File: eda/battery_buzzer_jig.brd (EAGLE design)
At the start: 47 x 26.7 mm, 12 parts, among them J2 AVR_SPI_PRG_6PTH

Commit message: Much tidying in pie.lbr
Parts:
- moved J2 0.54 mm to (4.45, 1.91)
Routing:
- net SCK: track 20.3 -> 20.8 mm
- net MOSI: track 22.0 -> 22.6 mm
- net MISO: track 16.7 -> 17.3 mm
- net RESET: track 37.9 -> 38.4 mm

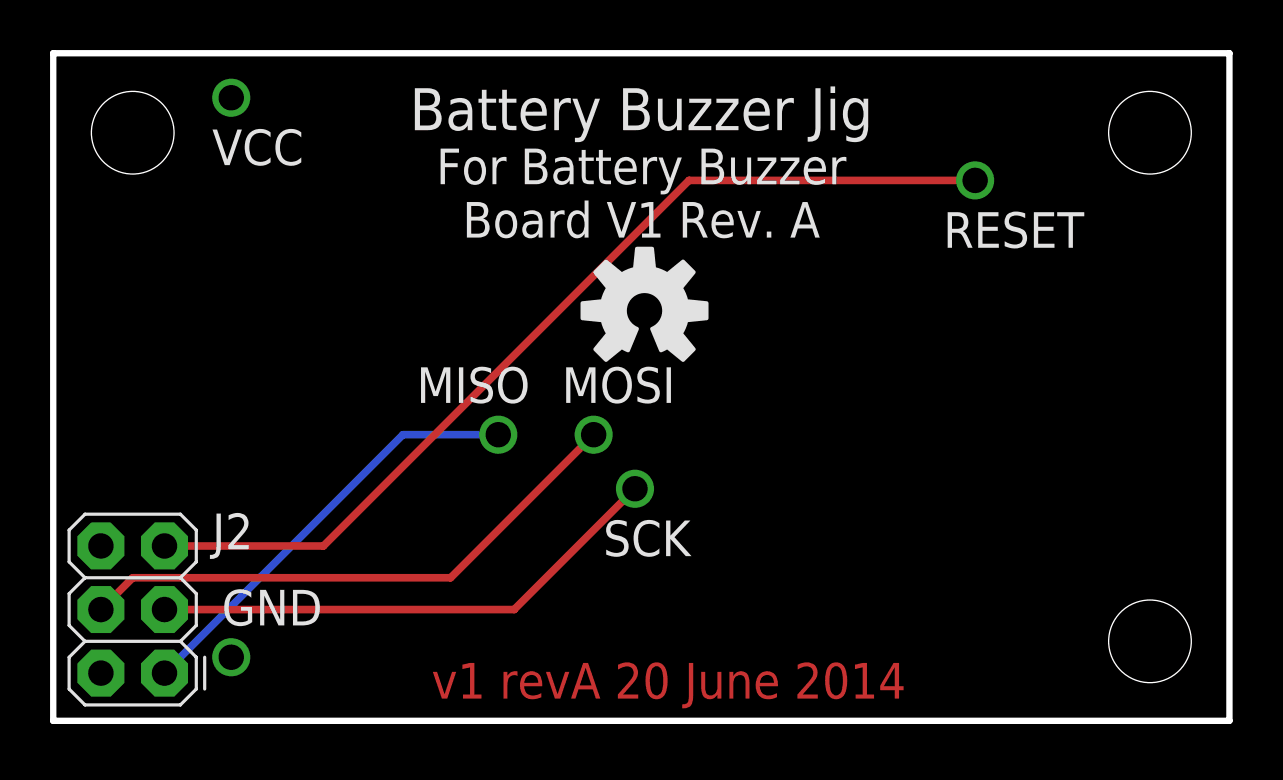
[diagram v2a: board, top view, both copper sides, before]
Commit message: All jigs probe vias accessible after populating.
Also changed "VCC" signal name on jigs to "5V" to match boards.
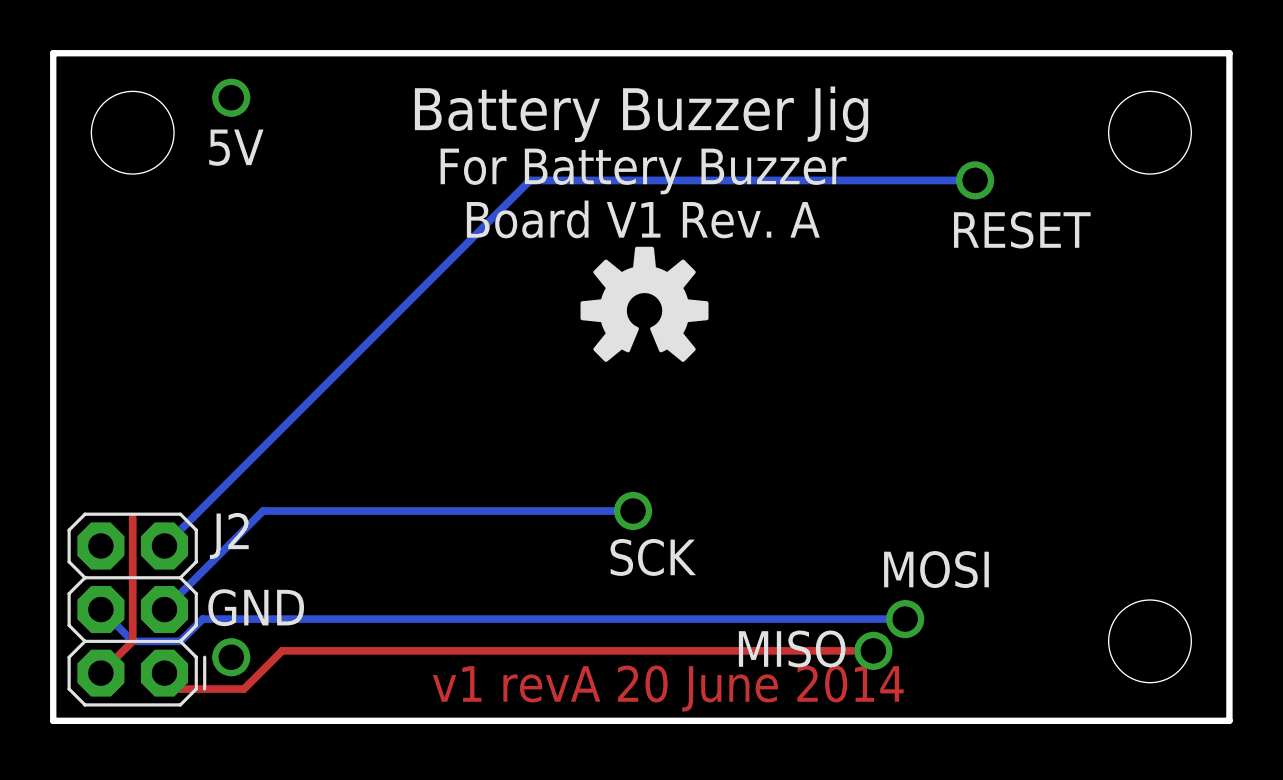
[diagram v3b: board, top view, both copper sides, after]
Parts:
- moved MISO 17.3 mm to (32.8, 2.79)
- moved MOSI 14.5 mm to (34.0, 4.06)
- moved SCK 0.89 mm to (23.2, 8.38)
- renumbered VCC to 5V
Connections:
- net VCC renamed 5V
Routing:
- net MISO: track 17.3 -> 29.2 mm
- net MOSI: track 22.6 -> 33.0 mm
- net 5V: track 0.00 -> 6.75 mm
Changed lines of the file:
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@@
 <text x="23.495" y="22.86" size="1.4224" layer="21" font="vector" ratio="15" align="top-center">For Battery Buzzer
 Board V1 Rev. A</text>
-<text x="15.113" y="0.889" size="1.4224" layer="1" font="vector" ratio="15">v1 revA 20 June 2014</text>
+<text x="15.113" y="0.762" size="1.4224" layer="1" font="vector" ratio="15">v1 revA 20 June 2014</text>
 </plain>
 <attributes>
@@
 <attribute name="PIE-INT-REF-NUM" value="BULK-STOCK" x="4.445" y="1.905" size="1.778" layer="27" rot="R90" display="off"/>
 </element>
-<element name="MISO" library="pie" package="POGO_PIN_394" value="" x="17.78" y="11.43" smashed="yes">
-<attribute name="NAME" x="19.05" y="12.7" size="1.4224" layer="25" font="vector" ratio="15" align="bottom-right"/>
-<attribute name="VALUE" x="16.51" y="8.89" size="1.27" layer="27" font="vector"/>
-<attribute name="PIE-INT-REF-NUM" value="POGO-PIN" x="17.78" y="11.43" size="1.778" layer="27" display="off"/>
-</element>
-<element name="SCK" library="pie" package="POGO_PIN_394" value="" x="23.241" y="9.271" smashed="yes">
-<attribute name="NAME" x="21.971" y="8.001" size="1.4224" layer="25" font="vector" ratio="15" align="top-left"/>
-<attribute name="VALUE" x="21.971" y="6.731" size="1.27" layer="27" font="vector"/>
-<attribute name="PIE-INT-REF-NUM" value="POGO-PIN" x="23.241" y="9.271" size="1.778" layer="27" display="off"/>
+<element name="MISO" library="pie" package="POGO_PIN_394" value="" x="32.766" y="2.794" smashed="yes">
+<attribute name="NAME" x="31.75" y="2.159" size="1.4224" layer="25" font="vector" ratio="15" align="bottom-right"/>
+<attribute name="VALUE" x="31.496" y="0.254" size="1.27" layer="27" font="vector"/>
+<attribute name="PIE-INT-REF-NUM" value="POGO-PIN" x="32.766" y="2.794" size="1.778" layer="27" display="off"/>
+</element>
+<element name="SCK" library="pie" package="POGO_PIN_394" value="" x="23.1648" y="8.382" smashed="yes">
+<attribute name="NAME" x="22.1488" y="7.239" size="1.4224" layer="25" font="vector" ratio="15" align="top-left"/>
+<attribute name="VALUE" x="21.8948" y="5.842" size="1.27" layer="27" font="vector"/>
+<attribute name="PIE-INT-REF-NUM" value="POGO-PIN" x="23.1648" y="8.382" size="1.778" layer="27" display="off"/>
 </element>
 <element name="RESET" library="pie" package="POGO_PIN_394" value="" x="36.83" y="21.59" smashed="yes" rot="R270">
-<attribute name="NAME" x="35.56" y="20.32" size="1.4224" layer="25" font="vector" ratio="15" align="top-left"/>
+<attribute name="NAME" x="35.814" y="20.32" size="1.4224" layer="25" font="vector" ratio="15" align="top-left"/>
 <attribute name="VALUE" x="34.29" y="22.86" size="1.27" layer="27" font="vector" rot="R270"/>
 <attribute name="PIE-INT-REF-NUM" value="POGO-PIN" x="36.83" y="21.59" size="1.778" layer="27" rot="R270" display="off"/>
 </element>
-<element name="VCC" library="pie" package="POGO_PIN_394" value="" x="7.112" y="24.892" smashed="yes" rot="R270">
-<attribute name="NAME" x="6.35" y="23.622" size="1.4224" layer="25" font="vector" ratio="15" align="top-left"/>
+<element name="5V" library="pie" package="POGO_PIN_394" value="" x="7.112" y="24.892" smashed="yes" rot="R270">
+<attribute name="NAME" x="6.096" y="23.622" size="1.4224" layer="25" font="vector" ratio="15" align="top-left"/>
 <attribute name="VALUE" x="4.572" y="26.162" size="1.27" layer="27" font="vector" rot="R270"/>
 <attribute name="PIE-INT-REF-NUM" value="POGO-PIN" x="7.112" y="24.892" size="1.778" layer="27" rot="R270" display="off"/>
 </element>
-<element name="MOSI" library="pie" package="POGO_PIN_394" value="" x="21.59" y="11.43" smashed="yes">
-<attribute name="NAME" x="20.32" y="12.7" size="1.4224" layer="25" font="vector" ratio="15"/>
-<attribute name="VALUE" x="20.32" y="8.89" size="1.27" layer="27" font="vector"/>
-<attribute name="PIE-INT-REF-NUM" value="POGO-PIN" x="21.59" y="11.43" size="1.778" layer="27" display="off"/>
+<element name="MOSI" library="pie" package="POGO_PIN_394" value="" x="34.036" y="4.064" smashed="yes">
+<attribute name="NAME" x="33.02" y="5.334" size="1.4224" layer="25" font="vector" ratio="15"/>
+<attribute name="VALUE" x="32.766" y="1.524" size="1.27" layer="27" font="vector"/>
+<attribute name="PIE-INT-REF-NUM" value="POGO-PIN" x="34.036" y="4.064" size="1.778" layer="27" display="off"/>
 </element>
 <element name="GND" library="pie" package="POGO_PIN_394" value="" x="7.112" y="2.54" smashed="yes" rot="R90">
-<attribute name="NAME" x="6.731" y="3.81" size="1.4224" layer="25" font="vector" ratio="15"/>
+<attribute name="NAME" x="6.096" y="3.81" size="1.4224" layer="25" font="vector" ratio="15"/>
 <attribute name="VALUE" x="9.652" y="1.27" size="1.27" layer="27" font="vector" rot="R90"/>
 <attribute name="PIE-INT-REF-NUM" value="POGO-PIN" x="7.112" y="2.54" size="1.778" layer="27" rot="R90" display="off"/>
@@
 <contactref element="J2" pad="4"/>
 <contactref element="MOSI" pad="POGO_PIN"/>
-<wire x1="1.905" y1="4.445" x2="3.175" y2="5.715" width="0.3048" layer="1"/>
-<wire x1="3.175" y1="5.715" x2="15.875" y2="5.715" width="0.3048" layer="1"/>
-<wire x1="15.875" y1="5.715" x2="21.59" y2="11.43" width="0.3048" layer="1"/>
-</signal>
-<signal name="VCC">
+<wire x1="1.905" y1="4.445" x2="3.175" y2="3.175" width="0.3048" layer="16"/>
+<wire x1="34.036" y1="4.064" x2="5.969" y2="4.064" width="0.3048" layer="16"/>
+<wire x1="5.969" y1="4.064" x2="5.08" y2="3.175" width="0.3048" layer="16"/>
+<wire x1="5.08" y1="3.175" x2="3.175" y2="3.175" width="0.3048" layer="16"/>
+</signal>
+<signal name="5V">
 <contactref element="J2" pad="2"/>
-<contactref element="VCC" pad="POGO_PIN"/>
+<contactref element="5V" pad="POGO_PIN"/>
 <polygon width="0.254" layer="1" isolate="0.3048">
 <vertex x="0" y="0"/>
@@
 <vertex x="46.99" y="0"/>
 </polygon>
+<wire x1="1.905" y1="1.905" x2="3.175" y2="3.175" width="0.3048" layer="1"/>
+<wire x1="3.175" y1="3.175" x2="3.175" y2="8.128" width="0.3048" layer="1"/>
 </signal>
 <signal name="RESET">
 <contactref element="J2" pad="5"/>
 <contactref element="RESET" pad="POGO_PIN"/>
-<wire x1="4.445" y1="6.985" x2="10.795" y2="6.985" width="0.3048" layer="1"/>
-<wire x1="10.795" y1="6.985" x2="25.4" y2="21.59" width="0.3048" layer="1"/>
-<wire x1="25.4" y1="21.59" x2="36.83" y2="21.59" width="0.3048" layer="1"/>
+<wire x1="36.83" y1="21.59" x2="19.05" y2="21.59" width="0.3048" layer="16"/>
+<wire x1="19.05" y1="21.59" x2="4.445" y2="6.985" width="0.3048" layer="16"/>
 </signal>
 <signal name="SCK">
 <contactref element="J2" pad="3"/>
 <contactref element="SCK" pad="POGO_PIN"/>
-<wire x1="4.445" y1="4.445" x2="18.415" y2="4.445" width="0.3048" layer="1"/>
-<wire x1="18.415" y1="4.445" x2="23.241" y2="9.271" width="0.3048" layer="1"/>
+<wire x1="23.1648" y1="8.382" x2="8.382" y2="8.382" width="0.3048" layer="16"/>
+<wire x1="8.382" y1="8.382" x2="4.445" y2="4.445" width="0.3048" layer="16"/>
 </signal>
 <signal name="MISO">
 <contactref element="J2" pad="1"/>
 <contactref element="MISO" pad="POGO_PIN"/>
-<wire x1="4.445" y1="1.905" x2="13.97" y2="11.43" width="0.3048" layer="16"/>
-<wire x1="13.97" y1="11.43" x2="17.78" y2="11.43" width="0.3048" layer="16"/>
+<wire x1="32.766" y1="2.794" x2="9.144" y2="2.794" width="0.3048" layer="1"/>
+<wire x1="9.144" y1="2.794" x2="7.62" y2="1.27" width="0.3048" layer="1"/>
+<wire x1="7.62" y1="1.27" x2="5.08" y2="1.27" width="0.3048" layer="1"/>
+<wire x1="5.08" y1="1.27" x2="4.445" y2="1.905" width="0.3048" layer="1"/>
 </signal>
 <signal name="A">
@@
 </signal>
 </signals>
+<errors>
+</errors>
 </board>
 </drawing>

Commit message: Standardized copyright and "Design by" info among boards.
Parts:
- moved U$2 0.63 mm to (23.5, 5.71)
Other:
- board text added: "(c) Pioneers in Engineering. Design by: Krystyn Neisess. This design is open source hardware. For more information, visit pioneers.berkeley.edu/opensource."
- board text removed: "(c) Pioneers in Engineering Design by: Krystyn Neisess This design is open source hardware. For more information visit pioneers.berkeley.edu/opensource"
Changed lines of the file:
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@@
 <wire x1="46.99" y1="26.67" x2="0" y2="26.67" width="0.254" layer="20"/>
 <wire x1="0" y1="26.67" x2="0" y2="0" width="0.254" layer="20"/>
-<text x="33.655" y="24.765" size="0.762" layer="22" font="vector" ratio="20" rot="SMR0" align="top-left">(c) Pioneers in Engineering
-Design by:
-Krystyn Neisess
+<text x="23.495" y="18.415" size="0.889" layer="22" font="vector" ratio="15" rot="SMR0" align="top-center">(c) Pioneers in Engineering.
+Design by:  Krystyn Neisess.
 This design is open source hardware.
-For more information visit
-pioneers.berkeley.edu/opensource</text>
+For more information, visit
+pioneers.berkeley.edu/opensource.</text>
 <text x="23.495" y="25.273" size="1.6764" layer="21" font="vector" ratio="15" align="top-center">Battery Buzzer Jig</text>
 <text x="23.495" y="22.86" size="1.4224" layer="21" font="vector" ratio="15" align="top-center">For Battery Buzzer
@@
 </element>
 <element name="U$1" library="pie" package="OSHW-LOGO-M" value="" x="23.622" y="16.383"/>
-<element name="U$2" library="pie" package="PIE-LOGO-SMALL" value="" x="23.495" y="5.08" rot="MR0"/>
+<element name="U$2" library="pie" package="PIE-LOGO-SMALL" value="" x="23.495" y="5.715" rot="MR0"/>
 <element name="U$3" library="pie" package="STAND-OFF" value="" x="43.815" y="3.175"/>
 <element name="U$4" library="pie" package="STAND-OFF" value="" x="3.175" y="23.495"/>

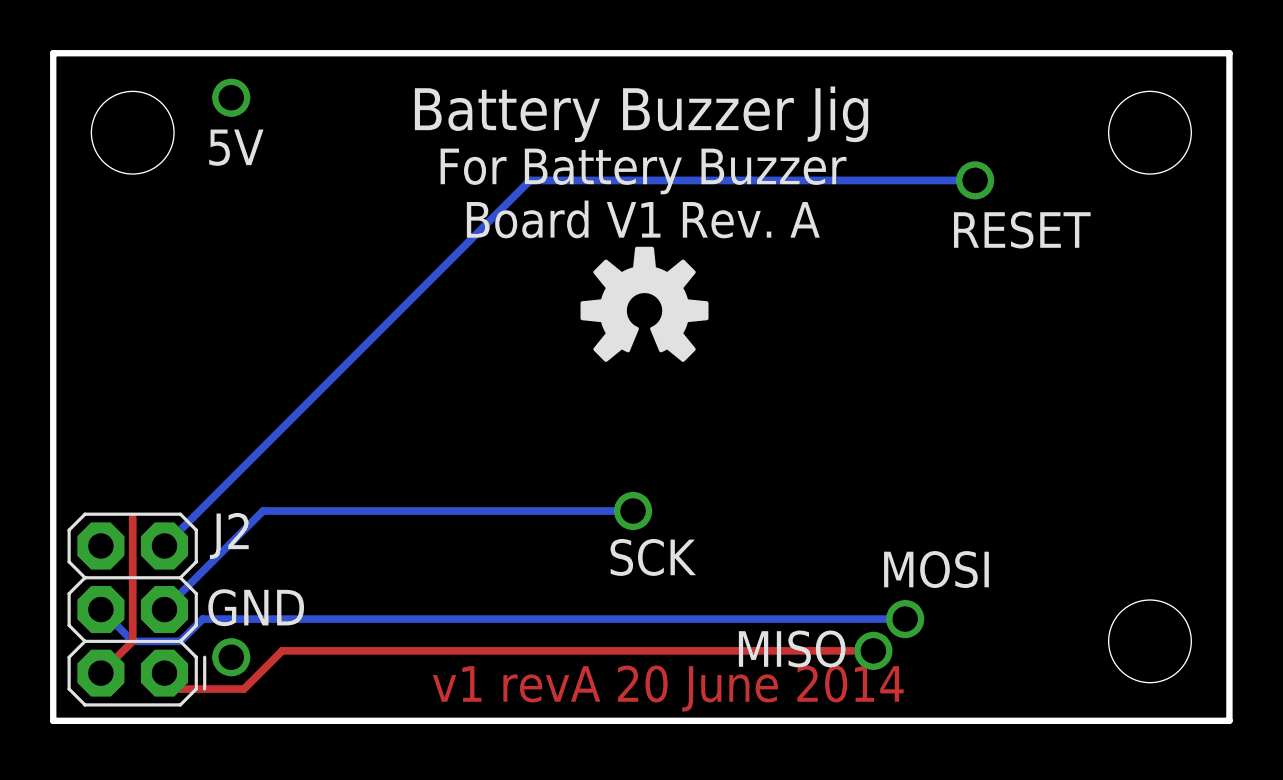
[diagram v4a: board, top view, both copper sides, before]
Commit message: Rerouted to accomodate 2x5 shrouded connector. On battery_buzzer, grizzly_bear, smartsensor, smartsensor_powered, and team_flag. Thanks Doug and Yizhe for helping!
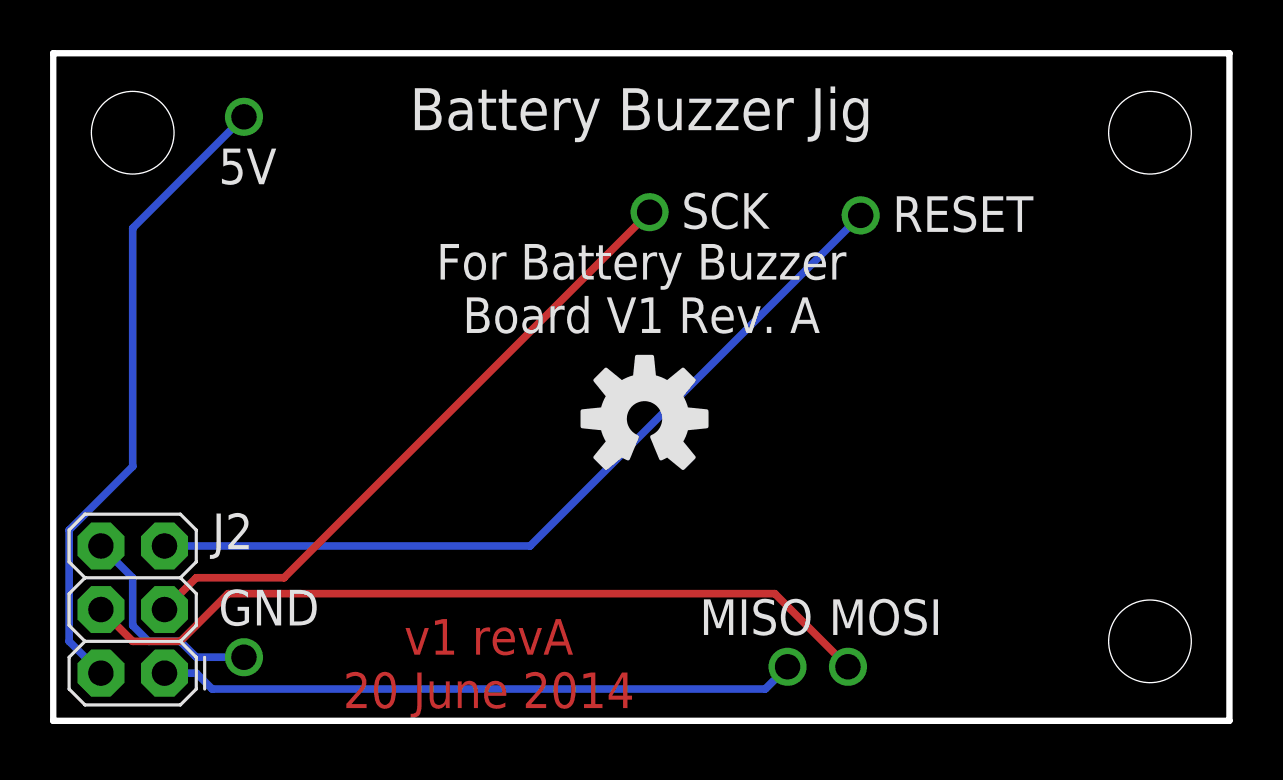
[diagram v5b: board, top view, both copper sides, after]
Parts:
- moved SCK 12.0 mm to (23.8, 20.3)
- moved RESET 4.78 mm to (32.3, 20.2)
- moved U$1 4.32 mm to (23.6, 12.1)
- moved MISO 3.49 mm to (29.3, 2.16)
- moved MOSI 2.98 mm to (31.8, 2.16)
- moved 5V 0.92 mm to (7.62, 24.1)
- moved GND 0.51 mm to (7.62, 2.54)
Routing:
- net 5V: track 6.75 -> 25.6 mm
- net A: track 0.00 -> 8.67 mm
- net SCK: track 20.4 -> 26.0 mm
- net RESET: track 38.4 -> 33.3 mm
- net MISO: track 29.2 -> 25.5 mm
- net MOSI: track 33.0 -> 32.4 mm

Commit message: battery buzzer and jig pogo pin changes/fixes
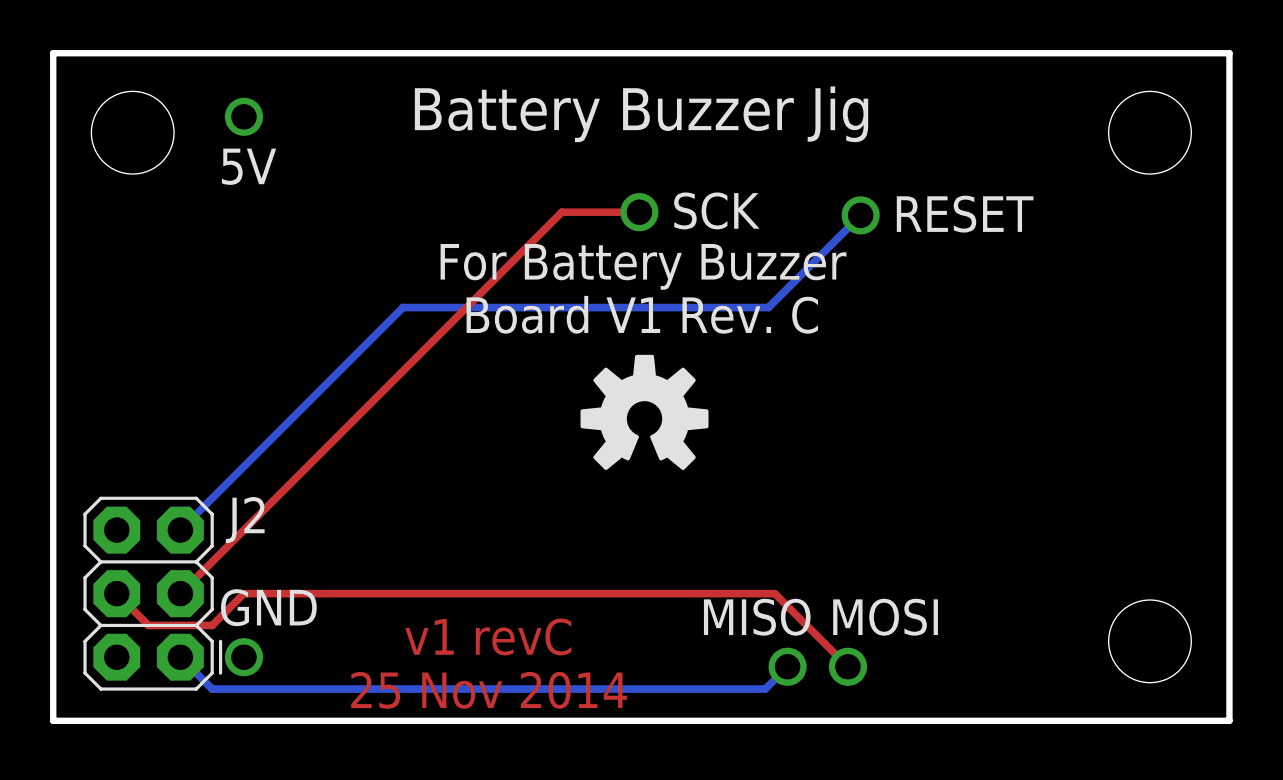
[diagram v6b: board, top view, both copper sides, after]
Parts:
- moved J2 0.90 mm to (5.08, 2.54)
- moved SCK 0.41 mm to (23.4, 20.3)
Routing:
- net 5V: track 25.6 -> 0.00 mm
- net A: track 8.67 -> 0.00 mm
- net SCK: track 26.0 -> 24.7 mm
- net MOSI: track 32.4 -> 31.5 mm
- net RESET: track 33.3 -> 32.4 mm
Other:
- board text added: "For Battery Buzzer Board V1 Rev. C"
- board text added: "v1 revC 25 Nov 2014"
- board text removed: "For Battery Buzzer Board V1 Rev. A"
- board text removed: "v1 revA 20 June 2014"
